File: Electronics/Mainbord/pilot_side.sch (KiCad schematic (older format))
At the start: 18 parts, among them U34 74HC165, U35 74HC165, U36 74HC165, U37 74HC165, U38 4067, U39 74HC4051, U40 74HC595

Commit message: Electronics - Misc works
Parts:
- added R? (x5): ?, symbol Device:R_Small
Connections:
- net CABIN: now also R?.1; no longer U40.3 (QD)
- net COM_1: now also R?.1; no longer U40.15 (QA)
- net COM_2: now also R?.1; no longer U40.1 (QB)
- net EMER: now also R?.1; no longer U40.4 (QE)
- net HF_1: now also R?.1; no longer U40.2 (QC)
- new net: R?.2, U40.1 (QB)
- new net: R?.2, U40.15 (QA)
- new net: R?.2, U40.2 (QC)
- new net: R?.2, U40.3 (QD)
- new net: R?.2, U40.4 (QE)
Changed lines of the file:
@@
 EESchema Schematic File Version 4
-LIBS:CitationX_cockpit-cache
-EELAYER 26 0
+EELAYER 30 0
 EELAYER END
 $Descr A4 8268 11693 portrait
 encoding utf-8
-Sheet 5 7
+Sheet 4 7
 Title ""
 Date ""
@@
 Text GLabel 5150 5800 0    50   Input ~ 0
 CLK
-Text Label 5950 5600 0    50   ~ 0
+Text Label 6150 5600 0    50   ~ 0
 COM_1
-Text Label 5950 5700 0    50   ~ 0
+Text Label 6150 5700 0    50   ~ 0
 COM_2
-Text Label 5950 5800 0    50   ~ 0
+Text Label 6150 5800 0    50   ~ 0
 HF_1
-Text Label 5950 5900 0    50   ~ 0
+Text Label 6150 5900 0    50   ~ 0
 CABIN
-Text Label 5950 6000 0    50   ~ 0
+Text Label 6150 6000 0    50   ~ 0
 EMER
 $Bitmap
@@
 EndData
 $EndBitmap
+$Comp
+L Device:R_Small R?
+U 1 1 5E00FD83
+P 6050 5600
+AR Path="/5DC33C09/5E00FD83" Ref="R?"  Part="1"
+AR Path="/5DC174D4/5E00FD83" Ref="R?"  Part="1"
+F 0 "R?" V 6000 5550 20  0000 C CNN
+F 1 "?" V 6050 5600 20  0000 C CNN
+F 2 "" H 6050 5600 50  0001 C CNN
+F 3 "~" H 6050 5600 50  0001 C CNN
+	1    6050 5600
+	0    1    1    0
+$EndComp
+$Comp
+L Device:R_Small R?
+U 1 1 5E012F05
+P 6050 5700
+AR Path="/5DC33C09/5E012F05" Ref="R?"  Part="1"
+AR Path="/5DC174D4/5E012F05" Ref="R?"  Part="1"
+F 0 "R?" V 6000 5650 20  0000 C CNN
+F 1 "?" V 6050 5700 20  0000 C CNN
+F 2 "" H 6050 5700 50  0001 C CNN
+F 3 "~" H 6050 5700 50  0001 C CNN
+	1    6050 5700
+	0    1    1    0
+$EndComp
+$Comp
+L Device:R_Small R?
+U 1 1 5E014C2B
+P 6050 5800
+AR Path="/5DC33C09/5E014C2B" Ref="R?"  Part="1"
+AR Path="/5DC174D4/5E014C2B" Ref="R?"  Part="1"
+F 0 "R?" V 6000 5750 20  0000 C CNN
+F 1 "?" V 6050 5800 20  0000 C CNN
+F 2 "" H 6050 5800 50  0001 C CNN
+F 3 "~" H 6050 5800 50  0001 C CNN
+	1    6050 5800
+	0    1    1    0
+$EndComp
+$Comp
+L Device:R_Small R?
+U 1 1 5E018213
+P 6050 5900
+AR Path="/5DC33C09/5E018213" Ref="R?"  Part="1"
+AR Path="/5DC174D4/5E018213" Ref="R?"  Part="1"
+F 0 "R?" V 6000 5850 20  0000 C CNN
+F 1 "?" V 6050 5900 20  0000 C CNN
+F 2 "" H 6050 5900 50  0001 C CNN
+F 3 "~" H 6050 5900 50  0001 C CNN
+	1    6050 5900
+	0    1    1    0
+$EndComp
+$Comp
+L Device:R_Small R?
+U 1 1 5E0183EA
+P 6050 6000
+AR Path="/5DC33C09/5E0183EA" Ref="R?"  Part="1"
+AR Path="/5DC174D4/5E0183EA" Ref="R?"  Part="1"
+F 0 "R?" V 6000 5950 20  0000 C CNN
+F 1 "?" V 6050 6000 20  0000 C CNN
+F 2 "" H 6050 6000 50  0001 C CNN
+F 3 "~" H 6050 6000 50  0001 C CNN
+	1    6050 6000
+	0    1    1    0
+$EndComp
 $EndSCHEMATC

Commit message: Electronics - Minor changes
Resistors to LEDs, transistors
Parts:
- removed C45: 0.1u, symbol Device:C_Small
- removed R? (x5): ?, symbol Device:R_Small
- removed RN18: R_Network08, Resistor_THT:R_Array_SIP9, symbol Device:R_Network08
- removed U37: 74HC165, symbol pkl_misc:74HC165
- added J? (x6): Screw_Terminal_01x10, symbol Connector:Screw_Terminal_01x10
- added R? (x5): R, symbol Device:R
- added U?: ULN2803A, symbol Transistor_Array:ULN2803A
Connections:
- net DOWN is gone; now on net ENT: RN16.4 (R3), U35.4 (D5)
- net LEFT is gone; now on net SKP: RN16.7 (R6), U35.13 (D2)
- net RIGHT is gone; now on net RCL: RN16.5 (R4), U35.3 (D4)
- net UP is gone; now on net PAG: RN16.6 (R5), U35.14 (D3)
- net +3V3: now also J?.10 (Pin_10)
- net ABN: now also J?.2 (Pin_2)
- net ACFT_SYS: now also J?.6 (Pin_6)
- net ADF_1: now also J?.7 (Pin_7)
- net ADF_2: now also J?.6 (Pin_6)
- net CABIN: now also J?.4 (Pin_4), R?.1
- net COM1_HP: now also J?.5 (Pin_5)
- net COM1_LSPK: now also J?.9 (Pin_9)
- net COM2_HP: now also J?.4 (Pin_4)
- net COM2_LSPK: now also J?.8 (Pin_8)
- net COM_1: now also J?.7 (Pin_7), R?.1
- net COM_2: now also J?.6 (Pin_6), R?.1
- net DME_1: now also J?.5 (Pin_5)
- net DME_2: now also J?.4 (Pin_4)
- net EMER: now also J?.1 (Pin_1), J?.3 (Pin_3), R?.1
- net ENT: now also J?.7 (Pin_7); no longer RN17.8 (R7), U36.12 (D1)
- net ET: now also J?.8 (Pin_8)
- net GND: now also J?.9 (Pin_9), U?.9 (GND)
- net HDPH: now also J?.8 (Pin_8)
- net HF_1: now also J?.3 (Pin_3), J?.5 (Pin_5), R?.1
- net INPH: now also J?.10 (Pin_10)
- net ISR_OUT: now also U36.9 (QH)
- net MFD_DIM: now also J?.6 (Pin_6)
- net MFD_MAP: now also J?.5 (Pin_5)
- net MFD_MX: now also J?.4 (Pin_4)
- net MIXER: now also J?.3 (Pin_3)
- net MKR: now also J?.9 (Pin_9)
- net MLS_1: now also J?.1 (Pin_1)
- net MLS_2: now also J?.10 (Pin_10)
- net NAV_1: now also J?.2 (Pin_2)
- net NAV_2: now also J?.1 (Pin_1)
- net NORM: now also J?.3 (Pin_3)
- net PAG: now also J?.9 (Pin_9); no longer RN16.2 (R1), U35.6 (D7)
- net PB_ADC_REV: now also RN17.4 (R3), U36.4 (D5), J?.9 (Pin_9)
- net PB_CABIN: now also RN17.8 (R7), U36.12 (D1), J?.3 (Pin_3); no longer RN17.4 (R3), U36.4 (D5)
- net PB_COM_1: now also RN16.3 (R2), U35.5 (D6), J?.6 (Pin_6); no longer RN17.7 (R6), U36.13 (D2)
- net PB_COM_2: now also RN16.2 (R1), U35.6 (D7), J?.5 (Pin_5); no longer RN17.6 (R5), U36.14 (D3)
- net PB_EMER: now also RN17.7 (R6), U36.13 (D2), J?.2 (Pin_2); no longer RN17.3 (R2), U36.5 (D6)
- net PB_HF_1: now also RN17.9 (R8), U36.11 (D0), J?.4 (Pin_4); no longer RN17.5 (R4), U36.3 (D4)
- net PB_IRS_REV: now also RN17.3 (R2), U36.5 (D6), J?.8 (Pin_8)
- net PB_MUTE: now also RN17.6 (R5), U36.14 (D3), J?.1 (Pin_1); no longer RN17.2 (R1), U36.6 (D7)
- net PB_SG_TEST: now also RN17.5 (R4), U36.3 (D4), J?.10 (Pin_10)
- net PFD_DIM: now also J?.7 (Pin_7)
- net PFD_HSI: now also J?.10 (Pin_10)
- net PFD_WXY: now also J?.9 (Pin_9)
- net RCL: now also J?.8 (Pin_8); no longer RN17.9 (R8), U36.11 (D0)
- net SKP: now also J?.10 (Pin_10); no longer RN16.3 (R2), U35.5 (D6)
- net SPKR: now also J?.2 (Pin_2)
- net TCAS: now also J?.7 (Pin_7)
- net at U40.1 (QB): now also U?.2 (I2)
- net at U40.15 (QA): now also U?.1 (I1)
- net at U40.2 (QC): now also U?.3 (I3)
- net at U40.3 (QD): now also U?.4 (I4)
- net at U40.4 (QE): now also U?.5 (I5)
- net at U40.5 (QF): now also U?.6 (I6)
- net at U40.6 (QG): now also U?.7 (I7)
- net at U40.7 (QH): now also U?.8 (I8)
- new net: RN17.2 (R1), U36.6 (D7)
- new net: R?.2, U?.10 (COM)
- new net: R?.2, U?.15 (O4)
- new net: R?.2, U?.16 (O3)
- new net: R?.2, U?.17 (O2)
- new net: R?.2, U?.18 (O1)
- new net SCL: J?.1 (Pin_1)
- new net SDA: J?.2 (Pin_2)
- no-connect marks 4 -> 3
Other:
- note added: "8-channel output shift register connected \nto Darlington transistor array for draining \ncurrent from LEDs"
- note added: "A/D converters"
- note removed: "8-channel output shift register"
- moved on the sheet: C46, U40

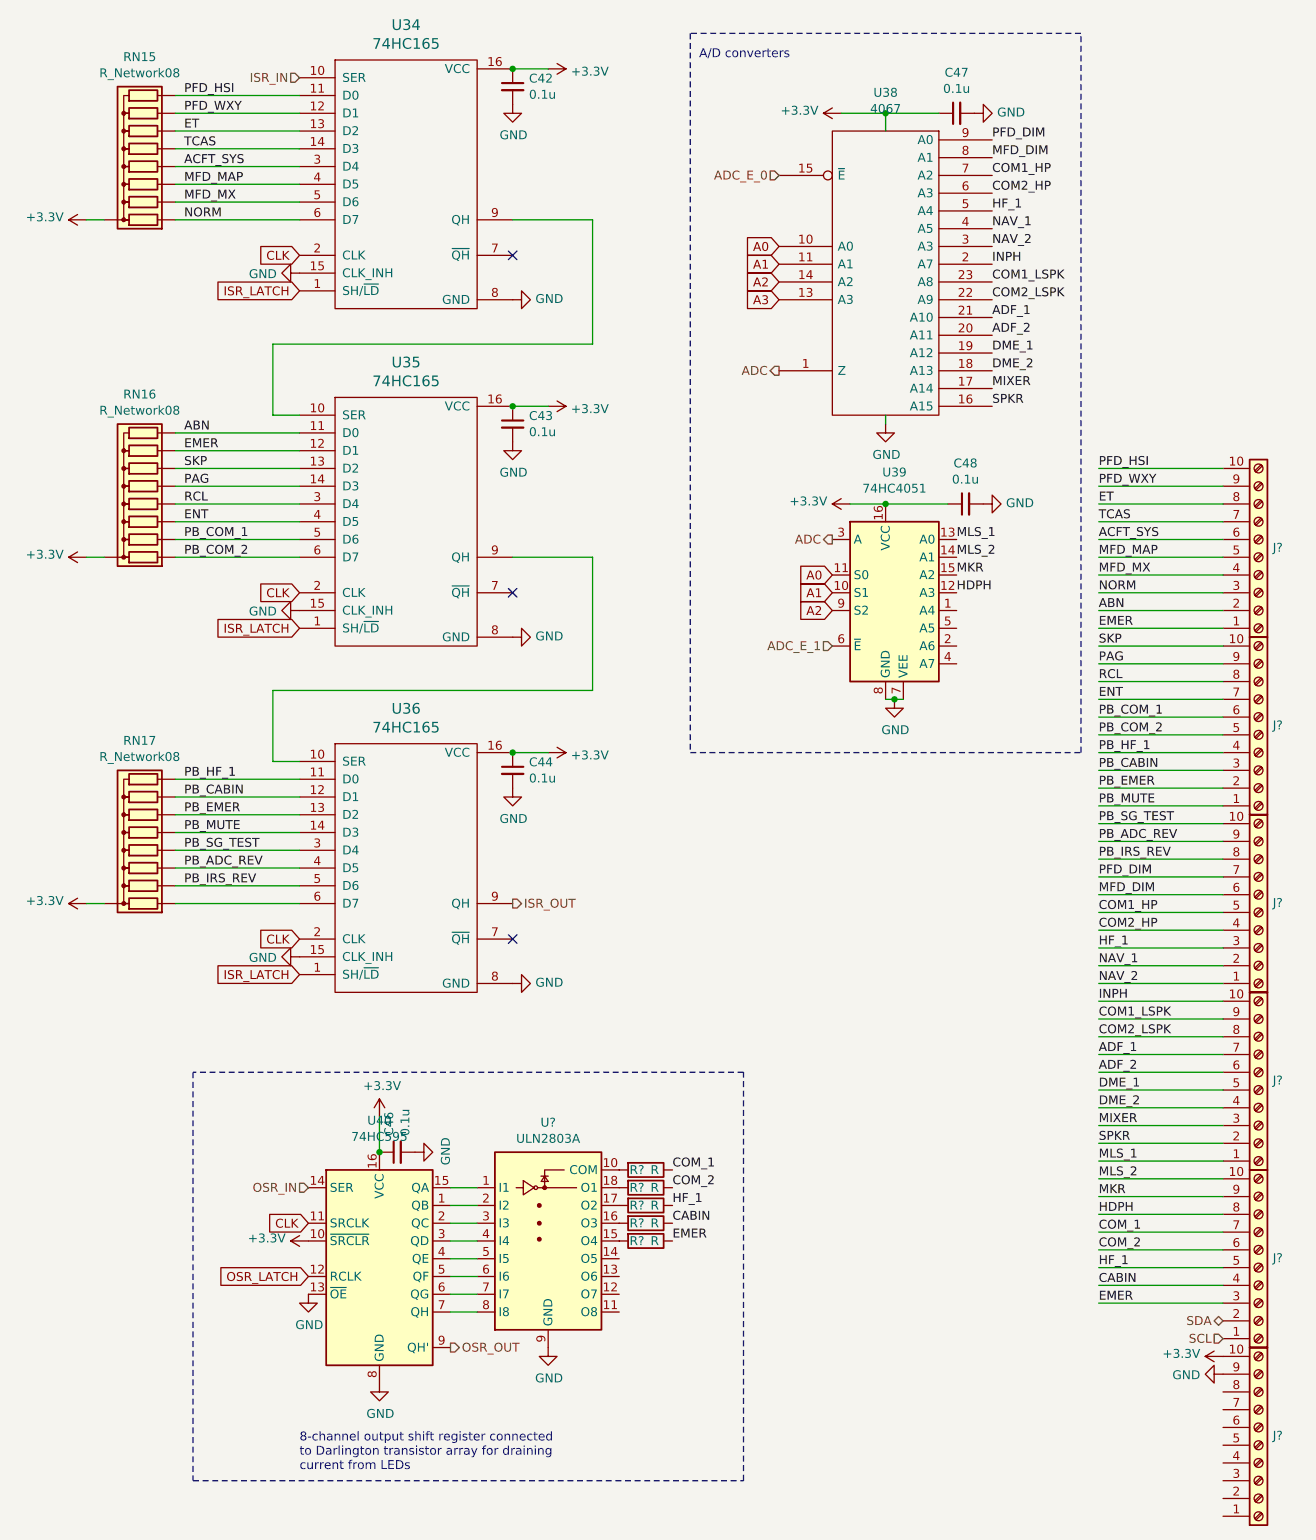
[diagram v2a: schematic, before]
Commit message: Electronics - Adds LCSC part numbers and footprints
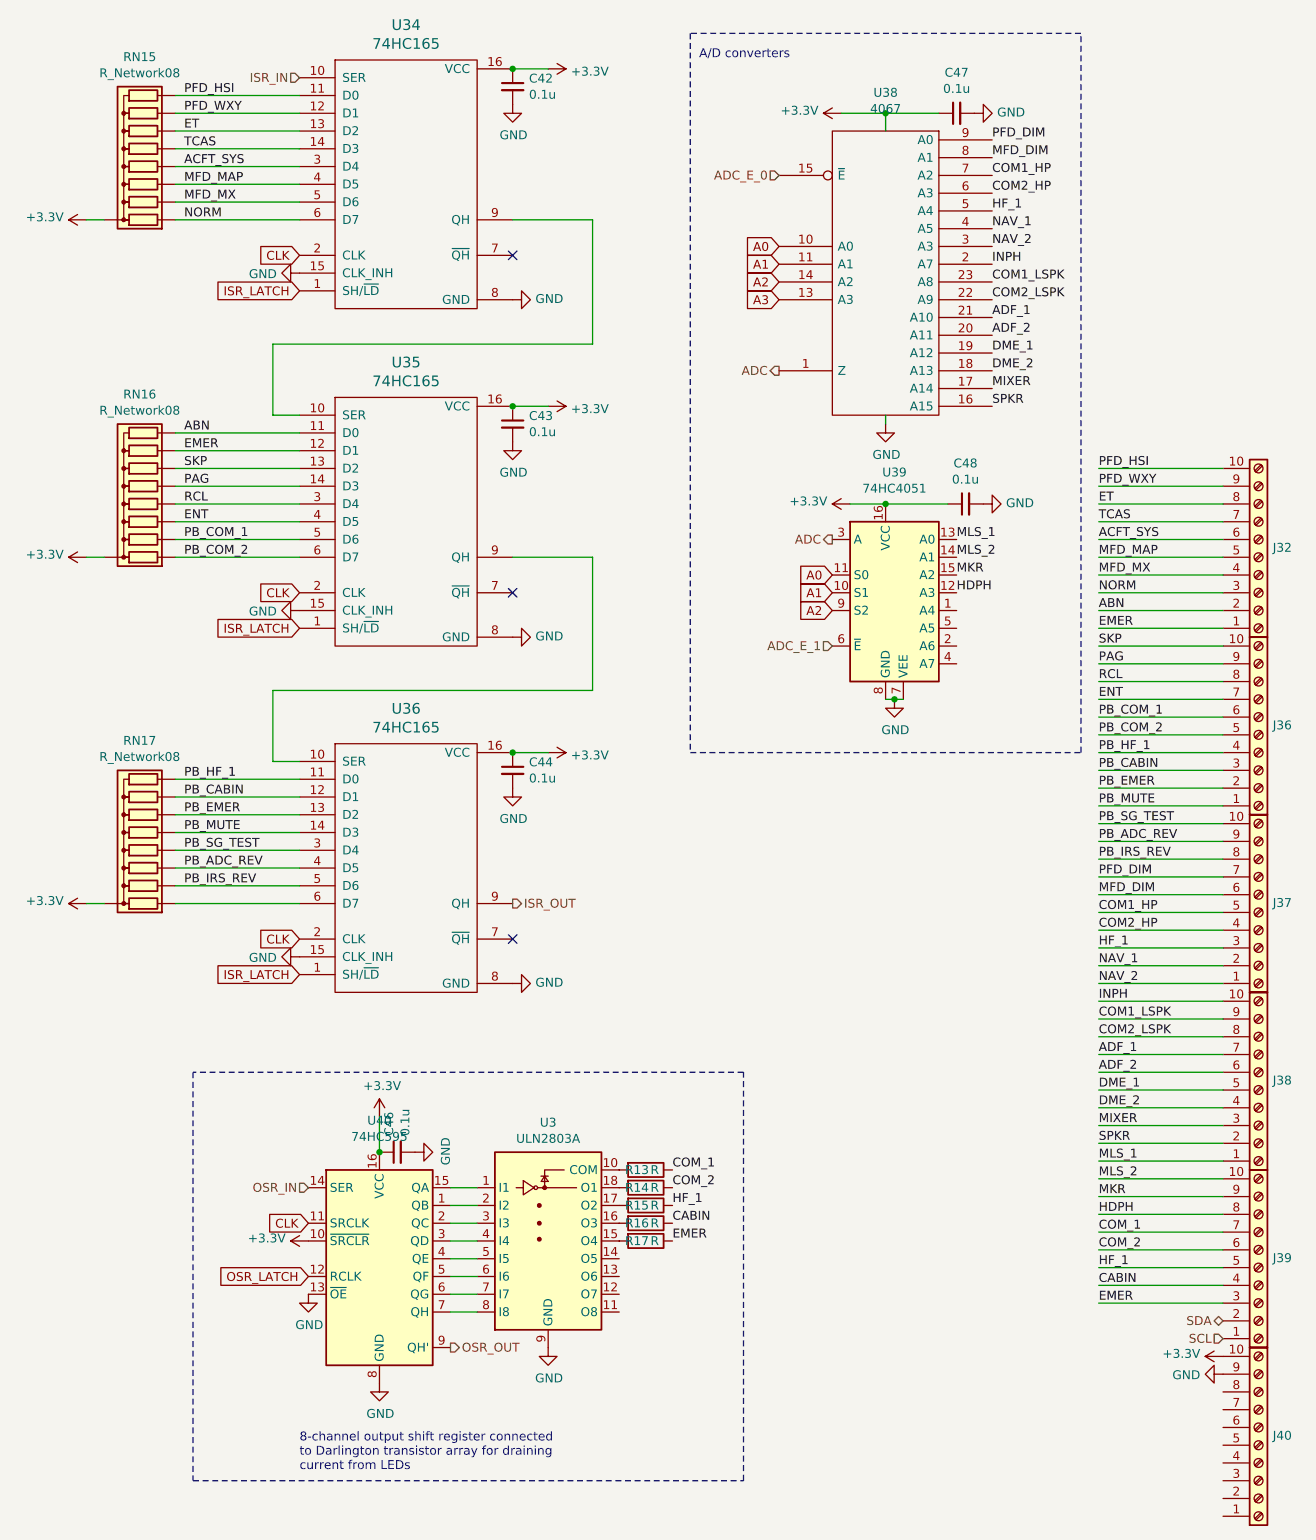
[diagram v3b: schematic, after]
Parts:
- gave numbers to parts that had none: 12
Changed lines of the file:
@@
 P 7650 3700
 AR Path="/5DB6029E/5DFA5F6C" Ref="J?"  Part="1"
-AR Path="/5DC174D4/5DFA5F6C" Ref="J?"  Part="1"
+AR Path="/5DC174D4/5DFA5F6C" Ref="J32"  Part="1"
 AR Path="/5DC31399/5DFA5F6C" Ref="J?"  Part="1"
-F 0 "J?" H 7730 3646 50  0000 L CNN
+F 0 "J32" H 7730 3646 50  0000 L CNN
 F 1 "Screw_Terminal_01x10" H 7570 3066 50  0001 C CNN
 F 2 "" H 7650 3700 50  0001 C CNN
@@
 P 7650 4700
 AR Path="/5DB6029E/5DFA5F83" Ref="J?"  Part="1"
-AR Path="/5DC174D4/5DFA5F83" Ref="J?"  Part="1"
+AR Path="/5DC174D4/5DFA5F83" Ref="J36"  Part="1"
 AR Path="/5DC31399/5DFA5F83" Ref="J?"  Part="1"
-F 0 "J?" H 7730 4646 50  0000 L CNN
+F 0 "J36" H 7730 4646 50  0000 L CNN
 F 1 "Screw_Terminal_01x10" H 7570 4066 50  0001 C CNN
 F 2 "" H 7650 4700 50  0001 C CNN
@@
 P 7650 5700
 AR Path="/5DB6029E/5DFA5FA9" Ref="J?"  Part="1"
-AR Path="/5DC174D4/5DFA5FA9" Ref="J?"  Part="1"
+AR Path="/5DC174D4/5DFA5FA9" Ref="J37"  Part="1"
 AR Path="/5DC31399/5DFA5FA9" Ref="J?"  Part="1"
-F 0 "J?" H 7730 5646 50  0000 L CNN
+F 0 "J37" H 7730 5646 50  0000 L CNN
 F 1 "Screw_Terminal_01x10" H 7570 5066 50  0001 C CNN
 F 2 "" H 7650 5700 50  0001 C CNN
@@
 P 7650 6700
 AR Path="/5DB6029E/5DFA5FB6" Ref="J?"  Part="1"
-AR Path="/5DC174D4/5DFA5FB6" Ref="J?"  Part="1"
+AR Path="/5DC174D4/5DFA5FB6" Ref="J38"  Part="1"
 AR Path="/5DC31399/5DFA5FB6" Ref="J?"  Part="1"
-F 0 "J?" H 7730 6646 50  0000 L CNN
+F 0 "J38" H 7730 6646 50  0000 L CNN
 F 1 "Screw_Terminal_01x10" H 7570 6066 50  0001 C CNN
 F 2 "" H 7650 6700 50  0001 C CNN
@@
 P 7650 7700
 AR Path="/5DB6029E/5DFA5FCD" Ref="J?"  Part="1"
-AR Path="/5DC174D4/5DFA5FCD" Ref="J?"  Part="1"
+AR Path="/5DC174D4/5DFA5FCD" Ref="J39"  Part="1"
 AR Path="/5DC31399/5DFA5FCD" Ref="J?"  Part="1"
-F 0 "J?" H 7730 7646 50  0000 L CNN
+F 0 "J39" H 7730 7646 50  0000 L CNN
 F 1 "Screw_Terminal_01x10" H 7570 7066 50  0001 C CNN
 F 2 "" H 7650 7700 50  0001 C CNN
@@
 P 7650 8700
 AR Path="/5DB6029E/5DFA5FDF" Ref="J?"  Part="1"
-AR Path="/5DC174D4/5DFA5FDF" Ref="J?"  Part="1"
+AR Path="/5DC174D4/5DFA5FDF" Ref="J40"  Part="1"
 AR Path="/5DC31399/5DFA5FDF" Ref="J?"  Part="1"
-F 0 "J?" H 7730 8646 50  0000 L CNN
+F 0 "J40" H 7730 8646 50  0000 L CNN
 F 1 "Screw_Terminal_01x10" H 7570 8066 50  0001 C CNN
 F 2 "" H 7650 8700 50  0001 C CNN
@@
 P 7450 8200
 AR Path="/5DB5DCD1/5DFA5FE8" Ref="#PWR?"  Part="1"
-AR Path="/5DC174D4/5DFA5FE8" Ref="#PWR?"  Part="1"
+AR Path="/5DC174D4/5DFA5FE8" Ref="#PWR0174"  Part="1"
 AR Path="/5DC31399/5DFA5FE8" Ref="#PWR?"  Part="1"
-F 0 "#PWR?" H 7450 8050 50  0001 C CNN
+F 0 "#PWR0174" H 7450 8050 50  0001 C CNN
 F 1 "+3.3V" V 7465 8328 50  0000 L CNN
 F 2 "" H 7450 8200 50  0001 C CNN
@@
 P 7450 8300
 AR Path="/5DB5DCD1/5DFA5FEE" Ref="#PWR?"  Part="1"
-AR Path="/5DC174D4/5DFA5FEE" Ref="#PWR?"  Part="1"
+AR Path="/5DC174D4/5DFA5FEE" Ref="#PWR0175"  Part="1"
 AR Path="/5DC31399/5DFA5FEE" Ref="#PWR?"  Part="1"
-F 0 "#PWR?" H 7450 8050 50  0001 C CNN
+F 0 "#PWR0175" H 7450 8050 50  0001 C CNN
 F 1 "GND" V 7455 8172 50  0000 R CNN
 F 2 "" H 7450 8300 50  0001 C CNN
@@
 AR Path="/5DC33C09/5DFC5BD5" Ref="U?"  Part="1"
 AR Path="/5DC31399/5DFC5BD5" Ref="U?"  Part="1"
-AR Path="/5DC174D4/5DFC5BD5" Ref="U?"  Part="1"
-F 0 "U?" H 3650 8017 50  0000 C CNN
+AR Path="/5DC174D4/5DFC5BD5" Ref="U3"  Part="1"
+F 0 "U3" H 3650 8017 50  0000 C CNN
 F 1 "ULN2803A" H 3650 7926 50  0000 C CNN
 F 2 "" H 3700 6800 50  0001 L CNN
@@
 P 3650 8150
 AR Path="/5DB5DCD1/5DFC5BDC" Ref="#PWR?"  Part="1"
-AR Path="/5DC174D4/5DFC5BDC" Ref="#PWR?"  Part="1"
+AR Path="/5DC174D4/5DFC5BDC" Ref="#PWR0182"  Part="1"
 AR Path="/5DC31399/5DFC5BDC" Ref="#PWR?"  Part="1"
-F 0 "#PWR?" H 3650 7900 50  0001 C CNN
+F 0 "#PWR0182" H 3650 7900 50  0001 C CNN
 F 1 "GND" H 3655 7977 50  0000 C CNN
 F 2 "" H 3650 8150 50  0001 C CNN
@@
 AR Path="/5DC33C09/5DFC5BE2" Ref="R?"  Part="1"
 AR Path="/5DC31399/5DFC5BE2" Ref="R?"  Part="1"
-AR Path="/5DC174D4/5DFC5BE2" Ref="R?"  Part="1"
-F 0 "R?" V 4200 7100 50  0000 C CNN
+AR Path="/5DC174D4/5DFC5BE2" Ref="R13"  Part="1"
+F 0 "R13" V 4200 7100 50  0000 C CNN
 F 1 "R" V 4200 7200 50  0000 C CNN
 F 2 "" V 4130 7150 50  0001 C CNN
@@
 AR Path="/5DC33C09/5DFC5BE9" Ref="R?"  Part="1"
 AR Path="/5DC31399/5DFC5BE9" Ref="R?"  Part="1"
-AR Path="/5DC174D4/5DFC5BE9" Ref="R?"  Part="1"
-F 0 "R?" V 4200 7200 50  0000 C CNN
+AR Path="/5DC174D4/5DFC5BE9" Ref="R14"  Part="1"
+F 0 "R14" V 4200 7200 50  0000 C CNN
 F 1 "R" V 4200 7300 50  0000 C CNN
 F 2 "" V 4130 7250 50  0001 C CNN
@@
 AR Path="/5DC33C09/5DFC5BF0" Ref="R?"  Part="1"
 AR Path="/5DC31399/5DFC5BF0" Ref="R?"  Part="1"
-AR Path="/5DC174D4/5DFC5BF0" Ref="R?"  Part="1"
-F 0 "R?" V 4200 7300 50  0000 C CNN
+AR Path="/5DC174D4/5DFC5BF0" Ref="R15"  Part="1"
+F 0 "R15" V 4200 7300 50  0000 C CNN
 F 1 "R" V 4200 7400 50  0000 C CNN
 F 2 "" V 4130 7350 50  0001 C CNN
@@
 AR Path="/5DC33C09/5DFC5BF7" Ref="R?"  Part="1"
 AR Path="/5DC31399/5DFC5BF7" Ref="R?"  Part="1"
-AR Path="/5DC174D4/5DFC5BF7" Ref="R?"  Part="1"
-F 0 "R?" V 4200 7400 50  0000 C CNN
+AR Path="/5DC174D4/5DFC5BF7" Ref="R16"  Part="1"
+F 0 "R16" V 4200 7400 50  0000 C CNN
 F 1 "R" V 4200 7500 50  0000 C CNN
 F 2 "" V 4130 7450 50  0001 C CNN
@@
 AR Path="/5DC33C09/5DFC5BFE" Ref="R?"  Part="1"
 AR Path="/5DC31399/5DFC5BFE" Ref="R?"  Part="1"
-AR Path="/5DC174D4/5DFC5BFE" Ref="R?"  Part="1"
-F 0 "R?" V 4200 7500 50  0000 C CNN
+AR Path="/5DC174D4/5DFC5BFE" Ref="R17"  Part="1"
+F 0 "R17" V 4200 7500 50  0000 C CNN
 F 1 "R" V 4200 7600 50  0000 C CNN
 F 2 "" V 4130 7550 50  0001 C CNN
